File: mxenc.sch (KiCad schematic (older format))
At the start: 34 parts, among them J10 Conn_02x05_Odd_Even, J4 Conn_01x06, J6 Conn_01x06, J8 Conn_01x04_MountingPin, SW1 SW_Push, SW2 SW_Push, U1 IMX8MM, U10 24C32, Y2 Crystal_GND24

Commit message: Add esd protection to cc lines
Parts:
- removed JP2: SolderJumper_2_Open, Jumper:SolderJumper-2_P1.3mm_Open_TrianglePad1.0x1.5mm, symbol Jumper:SolderJumper_2_Open
- added R49: 0 DNP, Resistor_SMD:R_0402_1005Metric, symbol Device:R
- R40: renamed from JP1; value SolderJumper_2_Open -> 0 DNP; footprint Jumper:SolderJumper-2_P1.3mm_Open_TrianglePad1.0x1.5mm -> Resistor_SMD:R_0402_1005Metric; symbol Jumper:SolderJumper_2_Open -> Device:R
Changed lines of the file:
@@
 	2400 4000 2550 4000
 $Comp
-L Jumper:SolderJumper_2_Open JP1
+L Device:R R40
 U 1 1 5F026C85
 P 2450 4350
-F 0 "JP1" V 2404 4418 50  0000 L CNN
-F 1 "SolderJumper_2_Open" V 2495 4418 50  0000 L CNN
-F 2 "Jumper:SolderJumper-2_P1.3mm_Open_TrianglePad1.0x1.5mm" H 2450 4350 50  0001 C CNN
+F 0 "R40" V 2550 4250 50  0000 L CNN
+F 1 "0 DNP" V 2550 4400 50  0000 L CNN
+F 2 "Resistor_SMD:R_0402_1005Metric" H 2450 4350 50  0001 C CNN
 F 3 "~" H 2450 4350 50  0001 C CNN
 	1    2450 4350
-	0    1    1    0
-$EndComp
-$Comp
-L Jumper:SolderJumper_2_Open JP2
-U 1 1 5F027943
-P 2550 4350
-F 0 "JP2" V 2504 4418 50  0000 L CNN
-F 1 "SolderJumper_2_Open" V 2595 4418 50  0000 L CNN
-F 2 "Jumper:SolderJumper-2_P1.3mm_Open_TrianglePad1.0x1.5mm" H 2550 4350 50  0001 C CNN
-F 3 "~" H 2550 4350 50  0001 C CNN
-	1    2550 4350
-	0    1    1    0
+	-1   0    0    1
 $EndComp
 Wire Wire Line
@@
 Text Label 5150 9950 0    50   ~ 0
 JTAG_TRST_B
+$Comp
+L Device:R R49
+U 1 1 5E4FE003
+P 2550 4350
+F 0 "R49" V 2450 4250 50  0000 L CNN
+F 1 "0 DNP" V 2450 4400 50  0000 L CNN
+F 2 "Resistor_SMD:R_0402_1005Metric" H 2550 4350 50  0001 C CNN
+F 3 "~" H 2550 4350 50  0001 C CNN
+	1    2550 4350
+	-1   0    0    1
+$EndComp
 $EndSCHEMATC

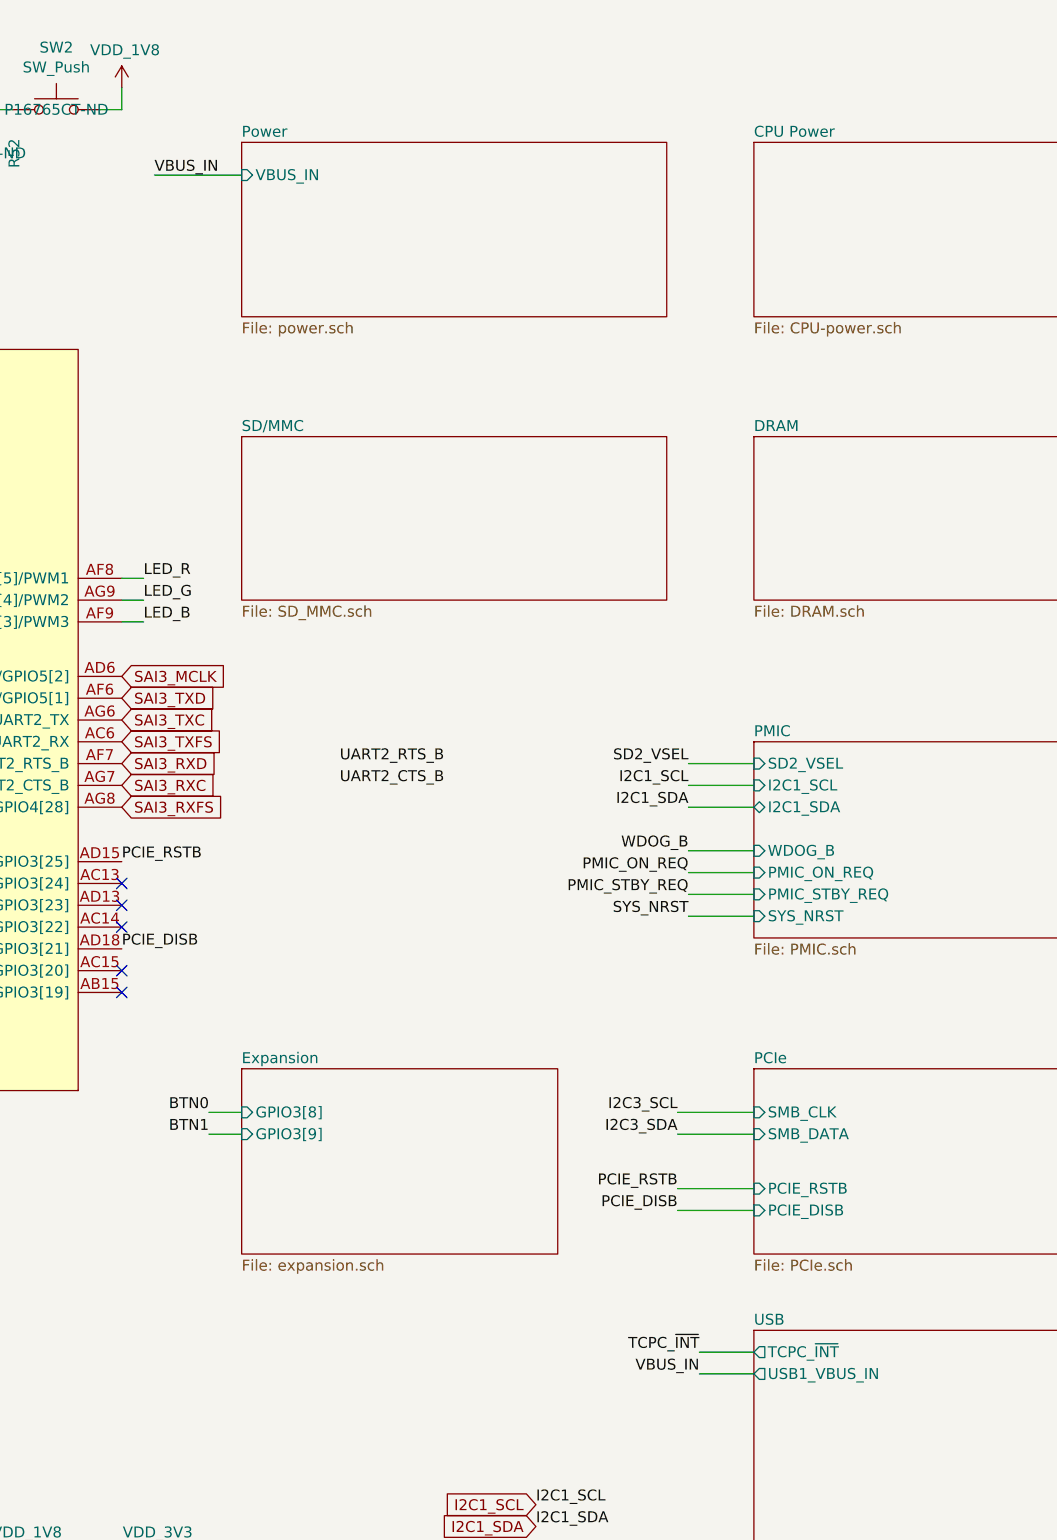
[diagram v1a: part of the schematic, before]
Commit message: Change power input to JST-PH
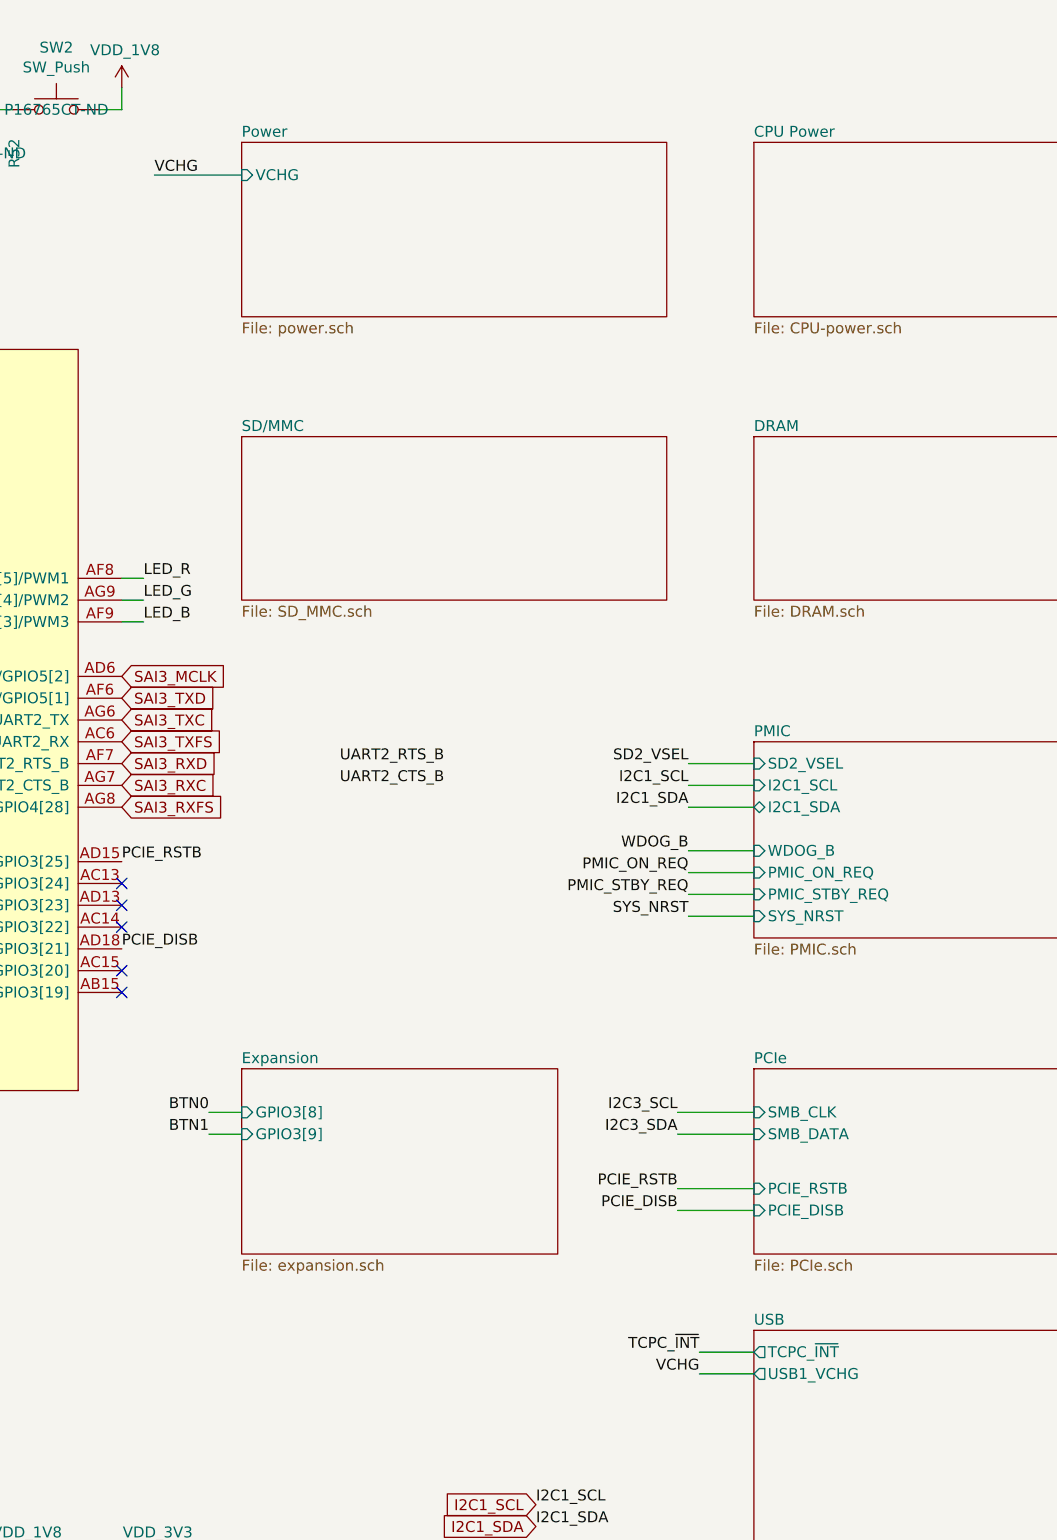
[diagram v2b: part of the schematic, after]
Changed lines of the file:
@@
 F0 "Power" 50
 F1 "power.sch" 50
-F2 "VBUS_IN" I L 11000 1450 50
+F2 "VCHG" I L 11000 1450 50
 $EndSheet
 Wire Wire Line
@@
 	13100 6950 13350 6950
 Text Label 13100 6950 2    50   ~ 0
-VBUS_IN
+VCHG
 Wire Wire Line
 	13000 5750 13350 5750
@@
 	10600 1450 11000 1450
 Text Label 10600 1450 0    50   ~ 0
-VBUS_IN
+VCHG
 $Sheet
 S 11000 2650 1950 750
@@
 F0 "USB" 50
 F1 "USB.sch" 50
-F2 "USB1_VBUS_IN" O L 13350 6950 50
+F2 "USB1_VCHG" O L 13350 6950 50
 F3 "USB1_PWR_SDA" B R 15400 7700 50
 F4 "USB1_PWR_SCL" I R 15400 7600 50

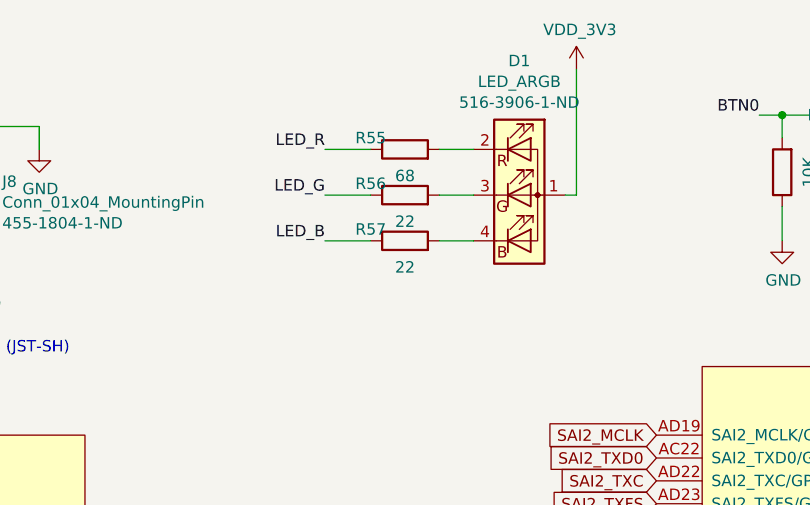
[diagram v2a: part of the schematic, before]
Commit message: Switch 5V buck for 1S battery charger boost
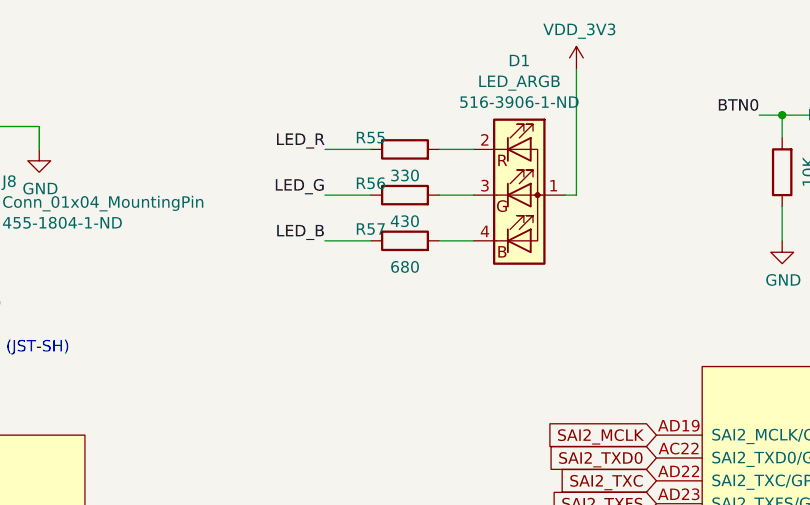
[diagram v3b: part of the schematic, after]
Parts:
- R55: value 68 -> 330; Part RC0201JR-0768RL -> RC0201JR-07330RL; Vendorpart YAG2364CT-ND -> 311-330NCT-ND
- R56: value 22 -> 430; Part RC0201JR-0722RL -> RC0201JR-07430RL; Vendorpart 311-22NCT-ND -> YAG2900CT-ND
- R57: value 22 -> 680; Part RC0201JR-0722RL -> RC0201JR-07680RL; Vendorpart 311-22NCT-ND -> 311-680NCT-ND
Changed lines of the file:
@@
 P 6800 1300
 F 0 "R55" V 6850 1450 50  0000 C CNN
-F 1 "68" V 6684 1300 50  0000 C CNN
+F 1 "330" V 6684 1300 50  0000 C CNN
 F 2 "Resistor_SMD:R_0201_0603Metric" V 6730 1300 50  0001 C CNN
 F 3 "~" H 6800 1300 50  0001 C CNN
 F 4 "Yageo" H 6800 1300 50  0001 C CNN "Mfgr"
-F 5 "RC0201JR-0768RL" H 6800 1300 50  0001 C CNN "Part"
-F 6 "YAG2364CT-ND" H 6800 1300 50  0001 C CNN "Vendorpart"
+F 5 "RC0201JR-07330RL" H 6800 1300 50  0001 C CNN "Part"
+F 6 "311-330NCT-ND" H 6800 1300 50  0001 C CNN "Vendorpart"
 	1    6800 1300
 	0    -1   -1   0
@@
 P 6800 1500
 F 0 "R56" V 6850 1650 50  0000 C CNN
-F 1 "22" V 6684 1500 50  0000 C CNN
+F 1 "430" V 6684 1500 50  0000 C CNN
 F 2 "Resistor_SMD:R_0201_0603Metric" V 6730 1500 50  0001 C CNN
 F 3 "~" H 6800 1500 50  0001 C CNN
 F 4 "Yageo" H 6800 1500 50  0001 C CNN "Mfgr"
-F 5 "RC0201JR-0722RL" H 6800 1500 50  0001 C CNN "Part"
-F 6 "311-22NCT-ND" H 6800 1500 50  0001 C CNN "Vendorpart"
+F 5 "RC0201JR-07430RL" H 6800 1500 50  0001 C CNN "Part"
+F 6 "YAG2900CT-ND" H 6800 1500 50  0001 C CNN "Vendorpart"
 	1    6800 1500
 	0    -1   -1   0
@@
 P 6800 1700
 F 0 "R57" V 6850 1850 50  0000 C CNN
-F 1 "22" V 6684 1700 50  0000 C CNN
+F 1 "680" V 6684 1700 50  0000 C CNN
 F 2 "Resistor_SMD:R_0201_0603Metric" V 6730 1700 50  0001 C CNN
 F 3 "~" H 6800 1700 50  0001 C CNN
 F 4 "Yageo" H 6800 1700 50  0001 C CNN "Mfgr"
-F 5 "RC0201JR-0722RL" H 6800 1700 50  0001 C CNN "Part"
-F 6 "311-22NCT-ND" H 6800 1700 50  0001 C CNN "Vendorpart"
+F 5 "RC0201JR-07680RL" H 6800 1700 50  0001 C CNN "Part"
+F 6 "311-680NCT-ND" H 6800 1700 50  0001 C CNN "Vendorpart"
 	1    6800 1700
 	0    -1   -1   0

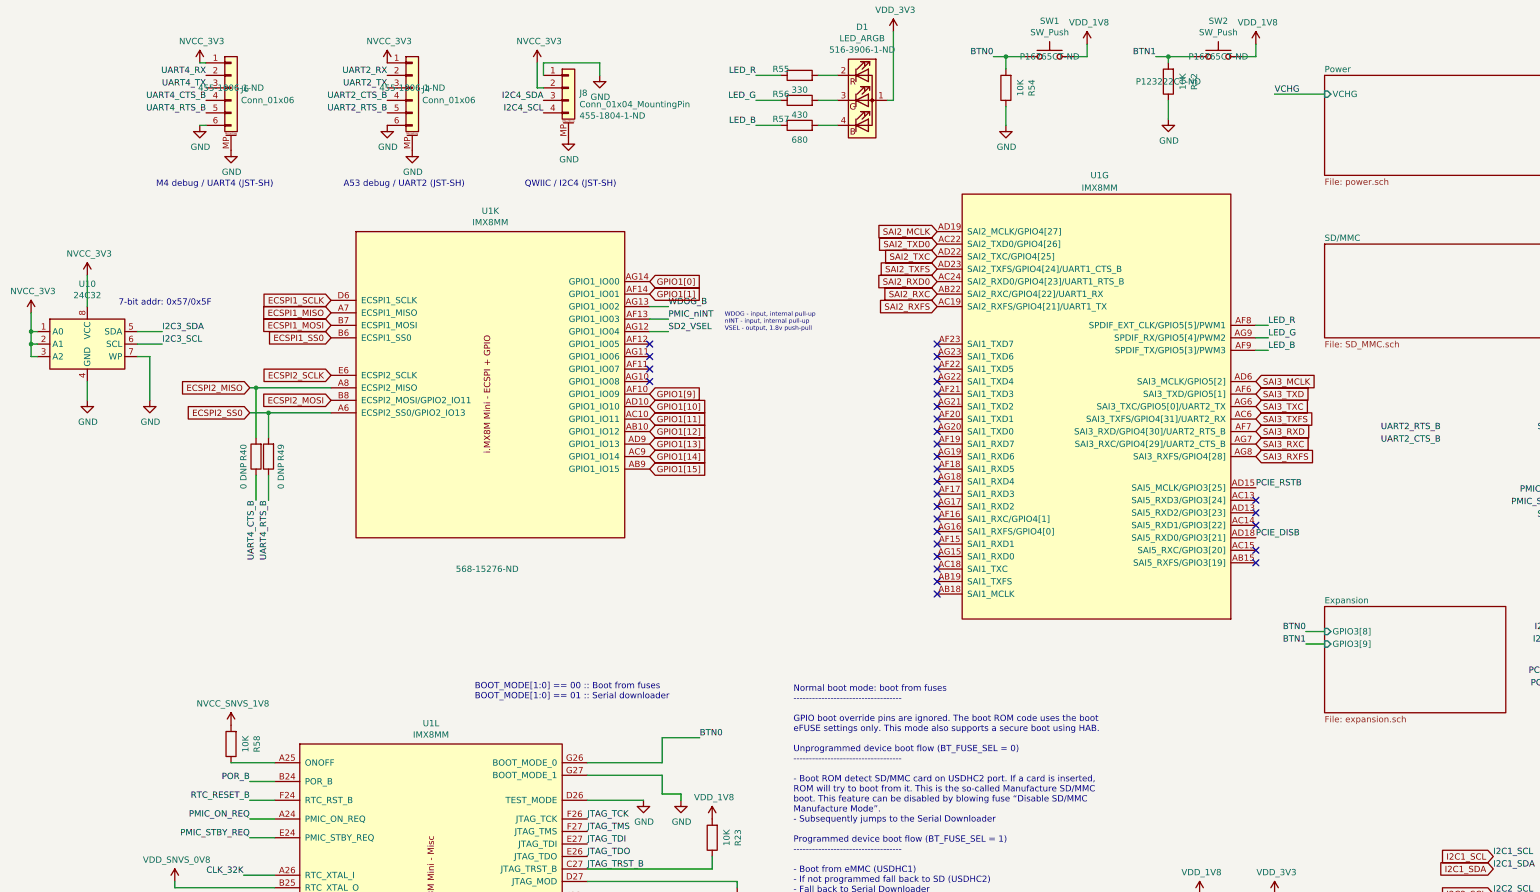
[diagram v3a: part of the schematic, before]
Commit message: Set up for battery NTC and add a power button
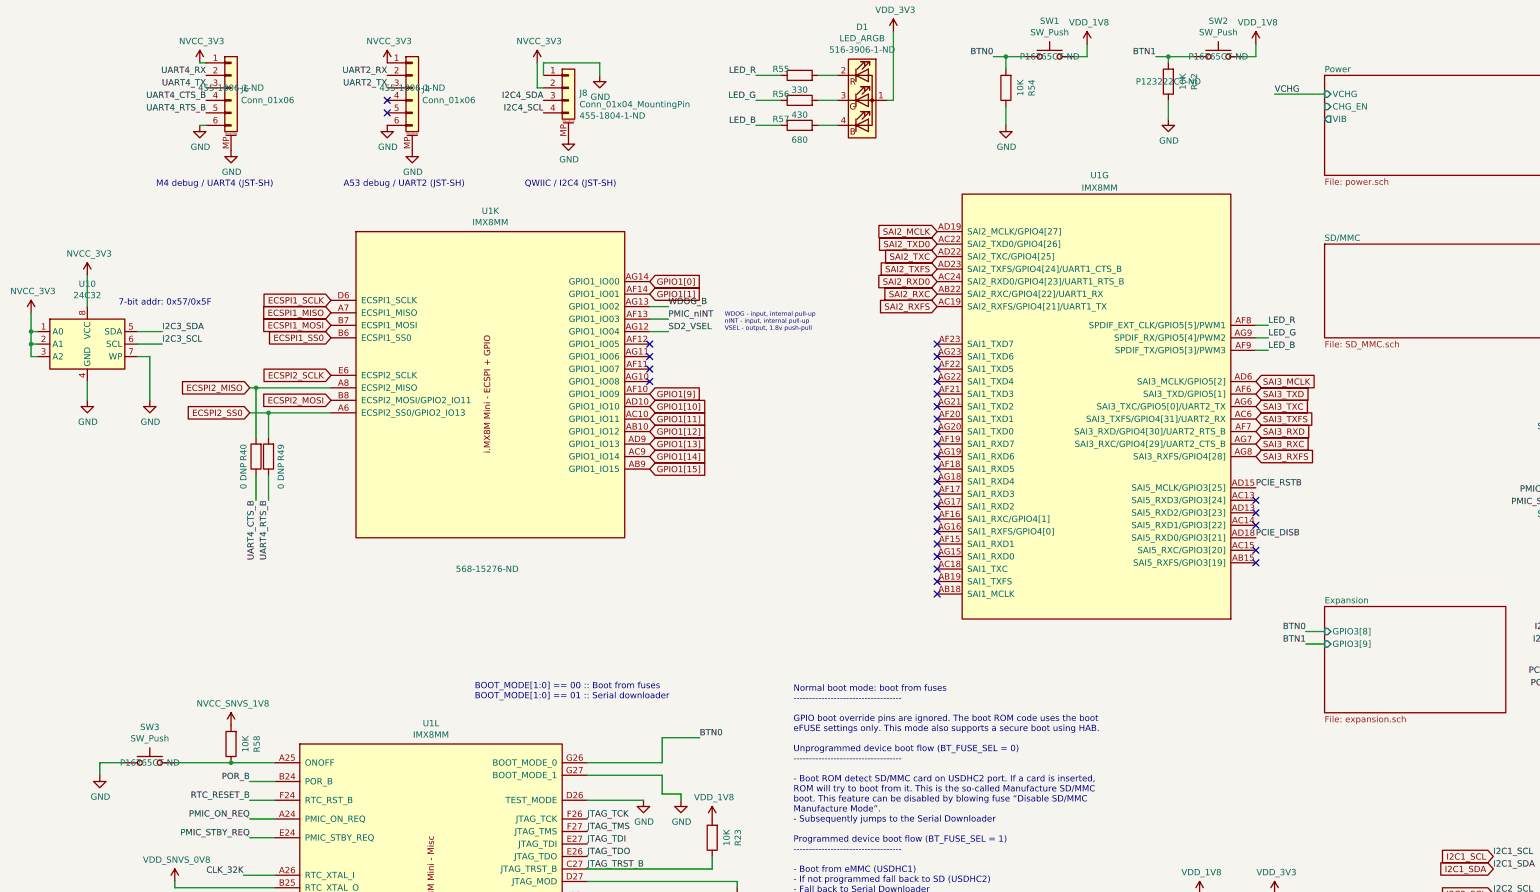
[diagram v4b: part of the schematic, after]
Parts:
- added SW3: SW_Push, mxenc:SW_SPST_EVQP7A, symbol Switch:SW_Push
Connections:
- net GND: now also SW3.1
- net at R58.1, U1.A25 (ONOFF): now also SW3.2
- net UART2_CTS_B: no longer names the net of J4.4 (Pin_4)
- net UART2_RTS_B: no longer names the net of J4.5 (Pin_5)
- no-connect marks 35 -> 37
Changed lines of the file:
@@
 EESchema Schematic File Version 4
-LIBS:mxenc-cache
-EELAYER 29 0
+EELAYER 30 0
 EELAYER END
 $Descr USLedger 17000 11000
 encoding utf-8
 Sheet 1 10
-Title ""
-Date ""
-Rev ""
-Comp ""
+Title "kimχ micro"
+Date "2020-03-05"
+Rev "0.9"
+Comp "GroupGets"
 Comment1 ""
 Comment2 ""
@@
 F1 "power.sch" 50
 F2 "VCHG" I L 11000 1450 50
+F3 "CHG_EN" I L 11000 1550 50
+F4 "VIB" O L 11000 1650 50
 $EndSheet
 Wire Wire Line
@@
 Text Label 7300 9100 2    50   ~ 0
 UART2_RX
-Text Label 11450 4150 0    50   ~ 0
-UART2_RTS_B
-Text Label 11450 4250 0    50   ~ 0
-UART2_CTS_B
 Text Label 3500 1400 2    50   ~ 0
 UART2_TX
 Text Label 3500 1300 2    50   ~ 0
 UART2_RX
-Text Label 3500 1600 2    50   ~ 0
-UART2_RTS_B
-Text Label 3500 1500 2    50   ~ 0
-UART2_CTS_B
 Text Label 2050 1400 2    50   ~ 0
 UART4_TX
@@
 	-1   0    0    1
 $EndComp
+$Comp
+L Switch:SW_Push SW3
+U 1 1 5E707050
+P 1600 6800
+F 0 "SW3" H 1600 7085 50  0000 C CNN
+F 1 "SW_Push" H 1600 6994 50  0000 C CNN
+F 2 "mxenc:SW_SPST_EVQP7A" H 1600 7000 50  0001 C CNN
+F 3 "~" H 1600 7000 50  0001 C CNN
+F 4 "P16765CT-ND" H 1600 6800 50  0000 C CNN "Vendorpart"
+F 5 "Panasonic" H 1600 6800 50  0001 C CNN "Mfgr"
+F 6 "EVQ-P7C01P" H 1600 6800 50  0001 C CNN "Part"
+	1    1600 6800
+	1    0    0    -1
+$EndComp
+$Comp
+L power:GND #PWR0276
+U 1 1 5E710EB8
+P 1200 6900
+F 0 "#PWR0276" H 1200 6650 50  0001 C CNN
+F 1 "GND" H 1205 6727 50  0000 C CNN
+F 2 "" H 1200 6900 50  0001 C CNN
+F 3 "" H 1200 6900 50  0001 C CNN
+	1    1200 6900
+	1    0    0    -1
+$EndComp
+Wire Wire Line
+	1200 6900 1200 6800
+Wire Wire Line
+	1200 6800 1400 6800
+Wire Wire Line
+	1800 6800 2250 6800
+Connection ~ 2250 6800
+NoConn ~ 3500 1500
+NoConn ~ 3500 1600
 $EndSCHEMATC
